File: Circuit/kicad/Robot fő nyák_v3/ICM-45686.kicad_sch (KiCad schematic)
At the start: 2 parts, among them U45 ICM-45686

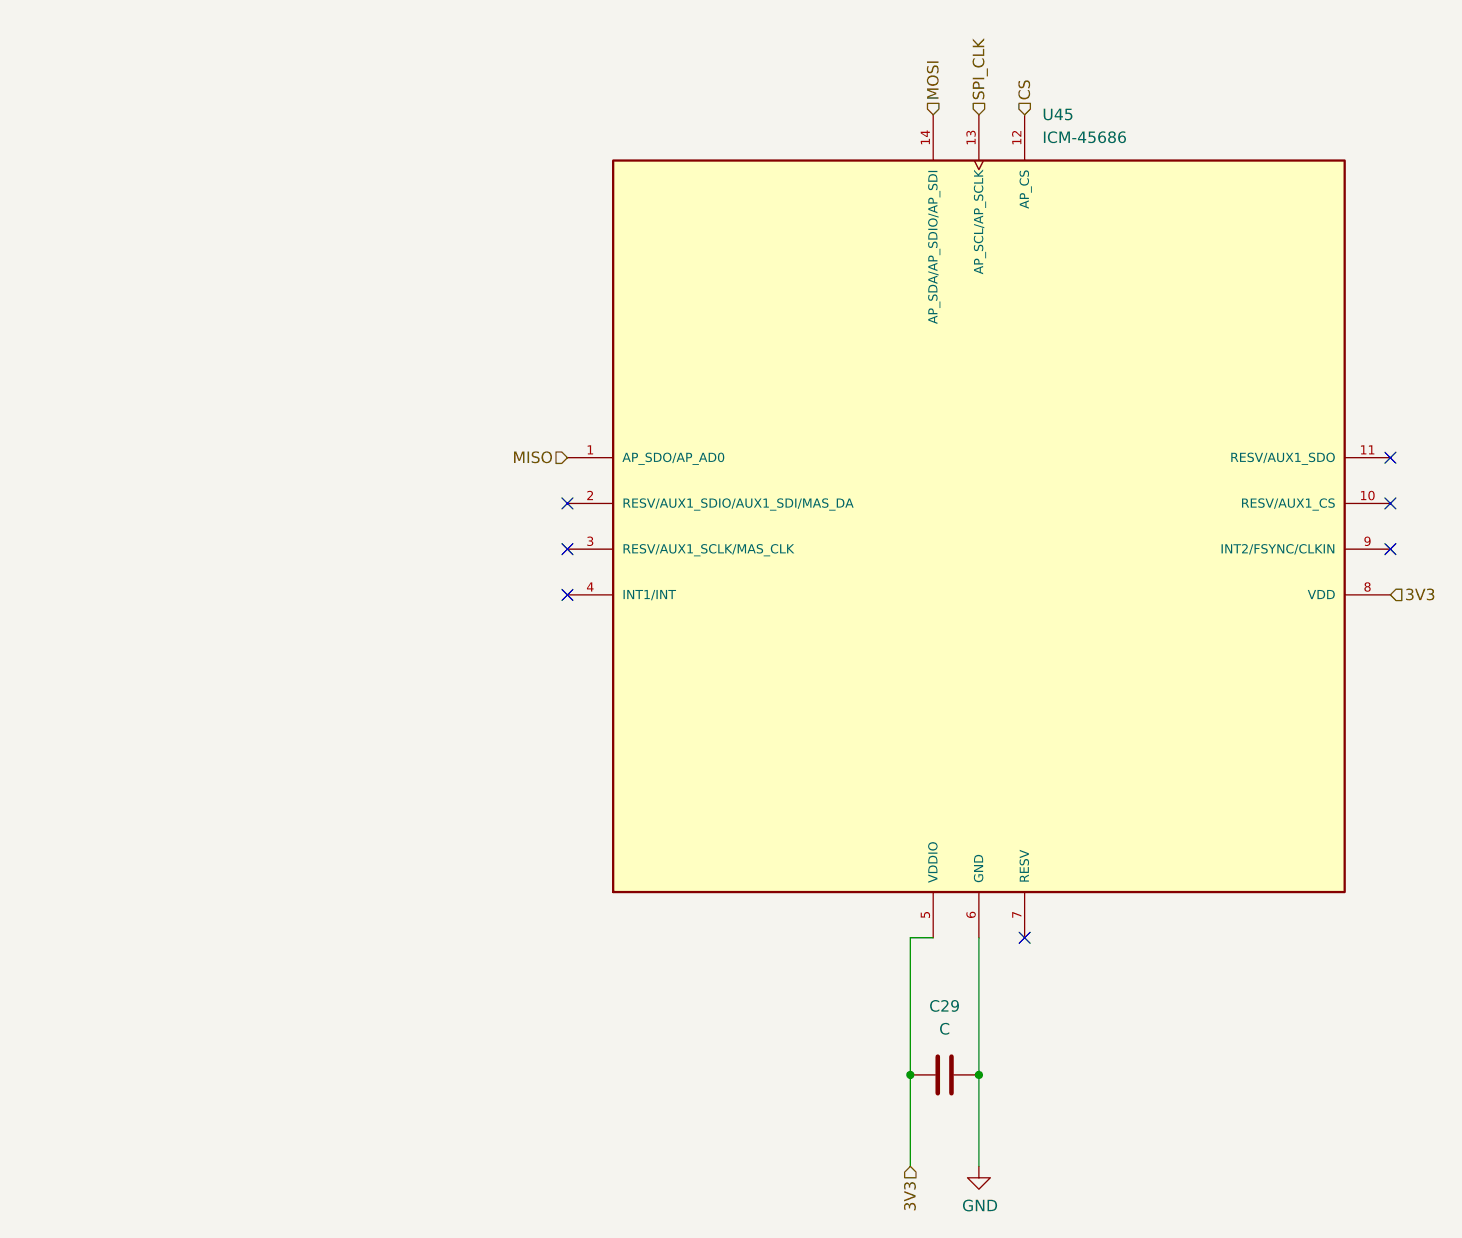
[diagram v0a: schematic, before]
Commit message: KICAD V3.01 Cleaned sheets + update + szekér modell add
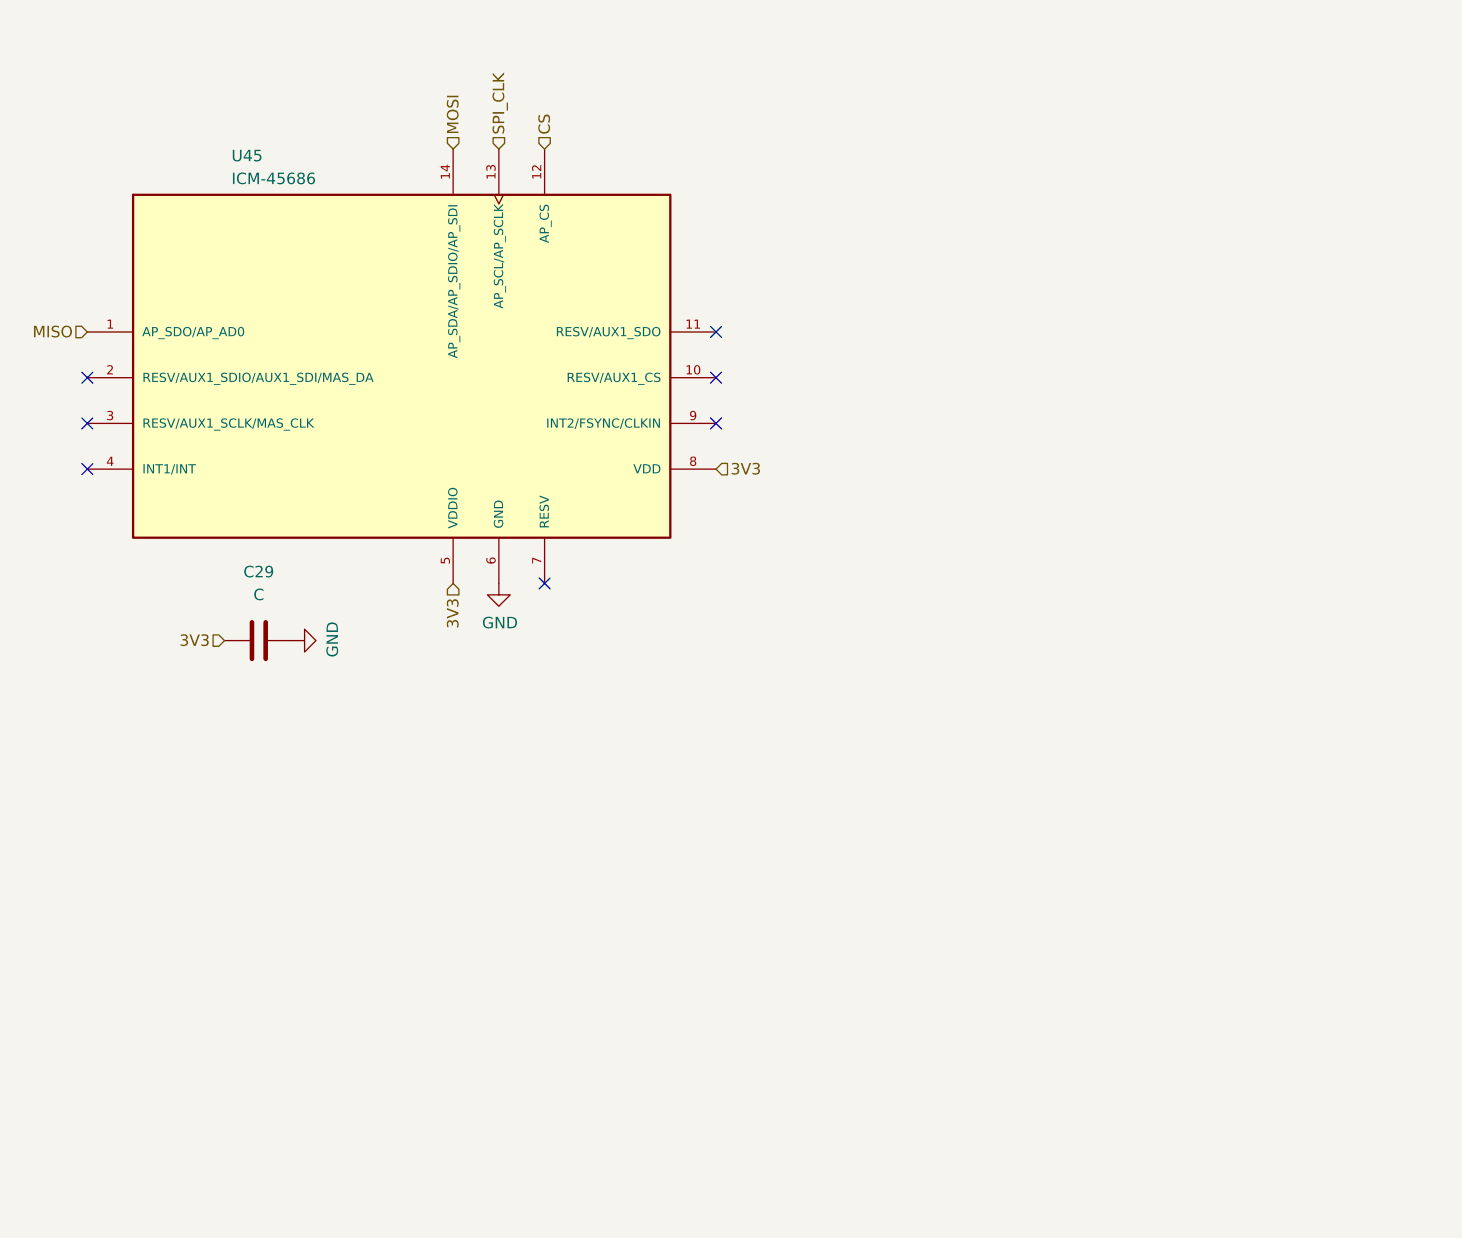
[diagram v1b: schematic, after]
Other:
- moved on the sheet: C29, U45
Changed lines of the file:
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@@
 	(generator "eeschema")
 	(generator_version "9.0")
-	(paper "A4")
-	(junction
-		(at 147.32 138.43)
-		(diameter 0)
-		(color 0 0 0 0)
-	)
-	(junction
-		(at 154.94 138.43)
-		(diameter 0)
-		(color 0 0 0 0)
-	)
+	(paper "A5")
 	(no_connect
-		(at 109.22 74.93)
+		(at 55.88 60.96)
 	)
 	(no_connect
-		(at 200.66 80.01)
+		(at 125.73 66.04)
 	)
 	(no_connect
-		(at 109.22 85.09)
+		(at 55.88 71.12)
 	)
 	(no_connect
-		(at 109.22 80.01)
+		(at 55.88 66.04)
 	)
 	(no_connect
-		(at 200.66 69.85)
+		(at 125.73 55.88)
 	)
 	(no_connect
-		(at 200.66 74.93)
+		(at 125.73 60.96)
 	)
 	(no_connect
-		(at 160.02 123.19)
-	)
-	(wire
-		(pts
-			(xy 149.86 123.19) (xy 147.32 123.19)
-		)
-		(stroke
-			(width 0)
-			(type default)
-		)
-	)
-	(wire
-		(pts
-			(xy 147.32 123.19) (xy 147.32 138.43)
-		)
-		(stroke
-			(width 0)
-			(type default)
-		)
-	)
-	(wire
-		(pts
-			(xy 154.94 123.19) (xy 154.94 138.43)
-		)
-		(stroke
-			(width 0)
-			(type default)
-		)
-	)
-	(wire
-		(pts
-			(xy 147.32 148.59) (xy 147.32 138.43)
-		)
-		(stroke
-			(width 0)
-			(type default)
-		)
-	)
-	(wire
-		(pts
-			(xy 154.94 148.59) (xy 154.94 138.43)
-		)
-		(stroke
-			(width 0)
-			(type default)
-		)
+		(at 106.68 83.82)
 	)
 	(image
@@
 	(hierarchical_label "MOSI"
 		(shape input)
-		(at 149.86 31.75 90)
+		(at 96.52 35.56 90)
 		(effects
 			(font
@@
 	(hierarchical_label "MISO"
 		(shape input)
-		(at 109.22 69.85 180)
+		(at 55.88 55.88 180)
 		(effects
 			(font
@@
 	(hierarchical_label "CS"
 		(shape input)
-		(at 160.02 31.75 90)
+		(at 106.68 35.56 90)
 		(effects
 			(font
@@
 	(hierarchical_label "3V3"
 		(shape input)
-		(at 200.66 85.09 0)
+		(at 125.73 71.12 0)
 		(effects
 			(font
@@
 	(hierarchical_label "3V3"
 		(shape input)
-		(at 147.32 148.59 270)
+		(at 96.52 83.82 270)
+		(effects
+			(font
+				(size 1.27 1.27)
+			)
+			(justify right)
+		)
+	)
+	(hierarchical_label "3V3"
+		(shape input)
+		(at 71.12 90.17 180)
 		(effects
 			(font
@@
 	(hierarchical_label "SPI_CLK"
 		(shape input)
-		(at 154.94 31.75 90)
+		(at 101.6 35.56 90)
 		(effects
 			(font
@@
 	(symbol
 		(lib_id "Device:C")
-		(at 151.13 138.43 90)
+		(at 74.93 90.17 90)
 		(unit 1)
 		(exclude_from_sim no)
@@
 		(fields_autoplaced yes)
 		(property "Reference" "C29"
-			(at 151.13 130.81 90)
+			(at 74.93 82.55 90)
 			(effects
 				(font
@@
 		)
 		(property "Value" "C"
-			(at 151.13 133.35 90)
+			(at 74.93 85.09 90)
 			(effects
 				(font
@@
 		)
 		(property "Footprint" "Capacitor_SMD:C_0805_2012Metric"
-			(at 154.94 137.4648 0)
+			(at 78.74 89.2048 0)
 			(effects
 				(font
@@
 		)
 		(property "Datasheet" "~"
-			(at 151.13 138.43 0)
+			(at 74.93 90.17 0)
 			(effects
 				(font
@@
 		)
 		(property "Description" "Unpolarized capacitor"
-			(at 151.13 138.43 0)
+			(at 74.93 90.17 0)
 			(effects
 				(font
@@
 		)
 		(instances
-			(project ""
+			(project "CM5IO"
 				(path "/e63e39d7-6ac0-4ffd-8aa3-1841a4541b55/a83afe30-5c7e-43cb-a5b2-f6f97a0812b3/86209e6a-92ae-4699-a125-02d46b525fc7/80185d9c-294a-4509-9bcc-8c38b499429e"
 					(reference "C29")
@@
 	(symbol
 		(lib_id "icm:ICM-45686")
-		(at 154.94 77.47 0)
+		(at 92.71 59.69 0)
 		(unit 1)
 		(exclude_from_sim no)
@@
 		(fields_autoplaced yes)
 		(property "Reference" "U45"
-			(at 161.9886 31.75 0)
+			(at 71.882 36.322 0)
 			(effects
 				(font
@@
 		)
 		(property "Value" "ICM-45686"
-			(at 161.9886 34.29 0)
+			(at 71.882 38.862 0)
 			(effects
 				(font
@@
 		)
 		(property "Footprint" "CM5IO:IC_ICM-45686"
-			(at 154.94 77.47 0)
+			(at 92.71 59.69 0)
 			(effects
 				(font
@@
 		)
 		(property "Datasheet" ""
-			(at 154.94 77.47 0)
+			(at 92.71 59.69 0)
 			(effects
 				(font
@@
 		)
 		(property "Description" ""
-			(at 154.94 77.47 0)
+			(at 92.71 59.69 0)
 			(effects
 				(font
@@
 		)
 		(property "PARTREV" "0.2"
-			(at 154.94 77.47 0)
+			(at 92.71 59.69 0)
 			(effects
 				(font
@@
 		)
 		(property "STANDARD" "Manufacturer Recommendations"
-			(at 154.94 77.47 0)
+			(at 92.71 59.69 0)
 			(effects
 				(font
@@
 		)
 		(property "MAXIMUM_PACKAGE_HEIGHT" "0.86mm"
-			(at 154.94 77.47 0)
+			(at 92.71 59.69 0)
 			(effects
 				(font
@@
 		)
 		(property "MANUFACTURER" "TDK InvenSense"
-			(at 154.94 77.47 0)
+			(at 92.71 59.69 0)
 			(effects
 				(font
@@
 	(symbol
 		(lib_id "power:GND")
-		(at 154.94 148.59 0)
+		(at 78.74 90.17 90)
+		(unit 1)
+		(exclude_from_sim no)
+		(in_bom yes)
+		(on_board yes)
+		(dnp no)
+		(property "Reference" "#PWR0149"
+			(at 85.09 90.17 0)
+			(effects
+				(font
+					(size 1.27 1.27)
+				)
+				(hide yes)
+			)
+		)
+		(property "Value" "GND"
+			(at 83.1342 90.043 0)
+			(effects
+				(font
+					(size 1.27 1.27)
+				)
+			)
+		)
+		(property "Footprint" ""
+			(at 78.74 90.17 0)
+			(effects
+				(font
+					(size 1.27 1.27)
+				)
+				(hide yes)
+			)
+		)
+		(property "Datasheet" ""
+			(at 78.74 90.17 0)
+			(effects
+				(font
+					(size 1.27 1.27)
+				)
+				(hide yes)
+			)
+		)
+		(property "Description" "Power symbol creates a global label with name \"GND\" , ground"
+			(at 78.74 90.17 0)
+			(effects
+				(font
+					(size 1.27 1.27)
+				)
+				(hide yes)
+			)
+		)
+		(pin "1"
+		)
+		(instances
+			(project "CM5IO"
+				(path "/e63e39d7-6ac0-4ffd-8aa3-1841a4541b55/a83afe30-5c7e-43cb-a5b2-f6f97a0812b3/86209e6a-92ae-4699-a125-02d46b525fc7/80185d9c-294a-4509-9bcc-8c38b499429e"
+					(reference "#PWR0149")
+					(unit 1)
+				)
+			)
+		)
+	)
+	(symbol
+		(lib_id "power:GND")
+		(at 101.6 83.82 0)
 		(unit 1)
 		(exclude_from_sim no)
@@
 		(dnp no)
 		(property "Reference" "#PWR0132"
-			(at 154.94 154.94 0)
+			(at 101.6 90.17 0)
 			(effects
 				(font
@@
 		)
 		(property "Value" "GND"
-			(at 155.067 152.9842 0)
+			(at 101.727 88.2142 0)
 			(effects
 				(font
@@
 		)
 		(property "Footprint" ""
-			(at 154.94 148.59 0)
+			(at 101.6 83.82 0)
 			(effects
 				(font
@@
 		)
 		(property "Datasheet" ""
-			(at 154.94 148.59 0)
+			(at 101.6 83.82 0)
 			(effects
 				(font
@@
 		)
 		(property "Description" "Power symbol creates a global label with name \"GND\" , ground"
-			(at 154.94 148.59 0)
+			(at 101.6 83.82 0)
 			(effects
 				(font

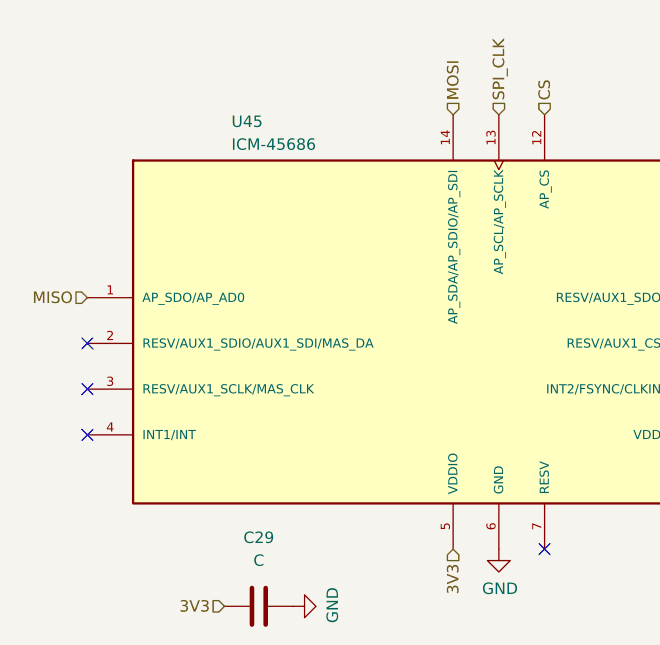
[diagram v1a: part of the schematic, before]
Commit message: kicad v0.1 footprint- assing spi finish
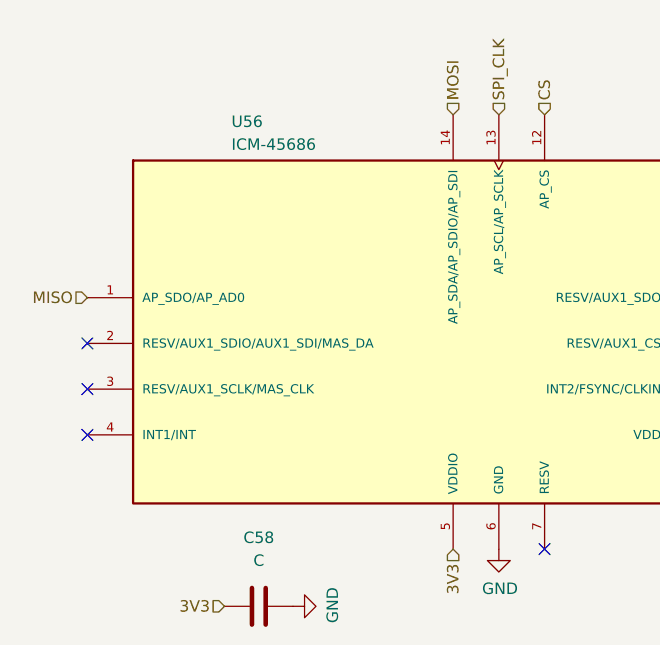
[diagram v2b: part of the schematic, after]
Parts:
- renumbered C29 to C58, U45 to U56
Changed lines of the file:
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@@
 		(dnp no)
 		(fields_autoplaced yes)
-		(property "Reference" "C29"
+		(property "Reference" "C58"
 			(at 74.93 82.55 90)
 			(effects
@@
 			(project "CM5IO"
 				(path "/e63e39d7-6ac0-4ffd-8aa3-1841a4541b55/a83afe30-5c7e-43cb-a5b2-f6f97a0812b3/86209e6a-92ae-4699-a125-02d46b525fc7/80185d9c-294a-4509-9bcc-8c38b499429e"
-					(reference "C29")
+					(reference "C58")
 					(unit 1)
 				)
@@
 		(dnp no)
 		(fields_autoplaced yes)
-		(property "Reference" "U45"
+		(property "Reference" "U56"
 			(at 71.882 36.322 0)
 			(effects
@@
 			(project ""
 				(path "/e63e39d7-6ac0-4ffd-8aa3-1841a4541b55/a83afe30-5c7e-43cb-a5b2-f6f97a0812b3/86209e6a-92ae-4699-a125-02d46b525fc7/80185d9c-294a-4509-9bcc-8c38b499429e"
-					(reference "U45")
+					(reference "U56")
 					(unit 1)
 				)
@@
 		(on_board yes)
 		(dnp no)
-		(property "Reference" "#PWR0149"
+		(property "Reference" "#PWR0125"
 			(at 85.09 90.17 0)
 			(effects
@@
 			(project "CM5IO"
 				(path "/e63e39d7-6ac0-4ffd-8aa3-1841a4541b55/a83afe30-5c7e-43cb-a5b2-f6f97a0812b3/86209e6a-92ae-4699-a125-02d46b525fc7/80185d9c-294a-4509-9bcc-8c38b499429e"
-					(reference "#PWR0149")
+					(reference "#PWR0125")
 					(unit 1)
 				)
@@
 		(on_board yes)
 		(dnp no)
-		(property "Reference" "#PWR0132"
+		(property "Reference" "#PWR0126"
 			(at 101.6 90.17 0)
 			(effects
@@
 			(project "CM5IO"
 				(path "/e63e39d7-6ac0-4ffd-8aa3-1841a4541b55/a83afe30-5c7e-43cb-a5b2-f6f97a0812b3/86209e6a-92ae-4699-a125-02d46b525fc7/80185d9c-294a-4509-9bcc-8c38b499429e"
-					(reference "#PWR0132")
+					(reference "#PWR0126")
 					(unit 1)
 				)
